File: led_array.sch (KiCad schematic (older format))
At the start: 41 parts

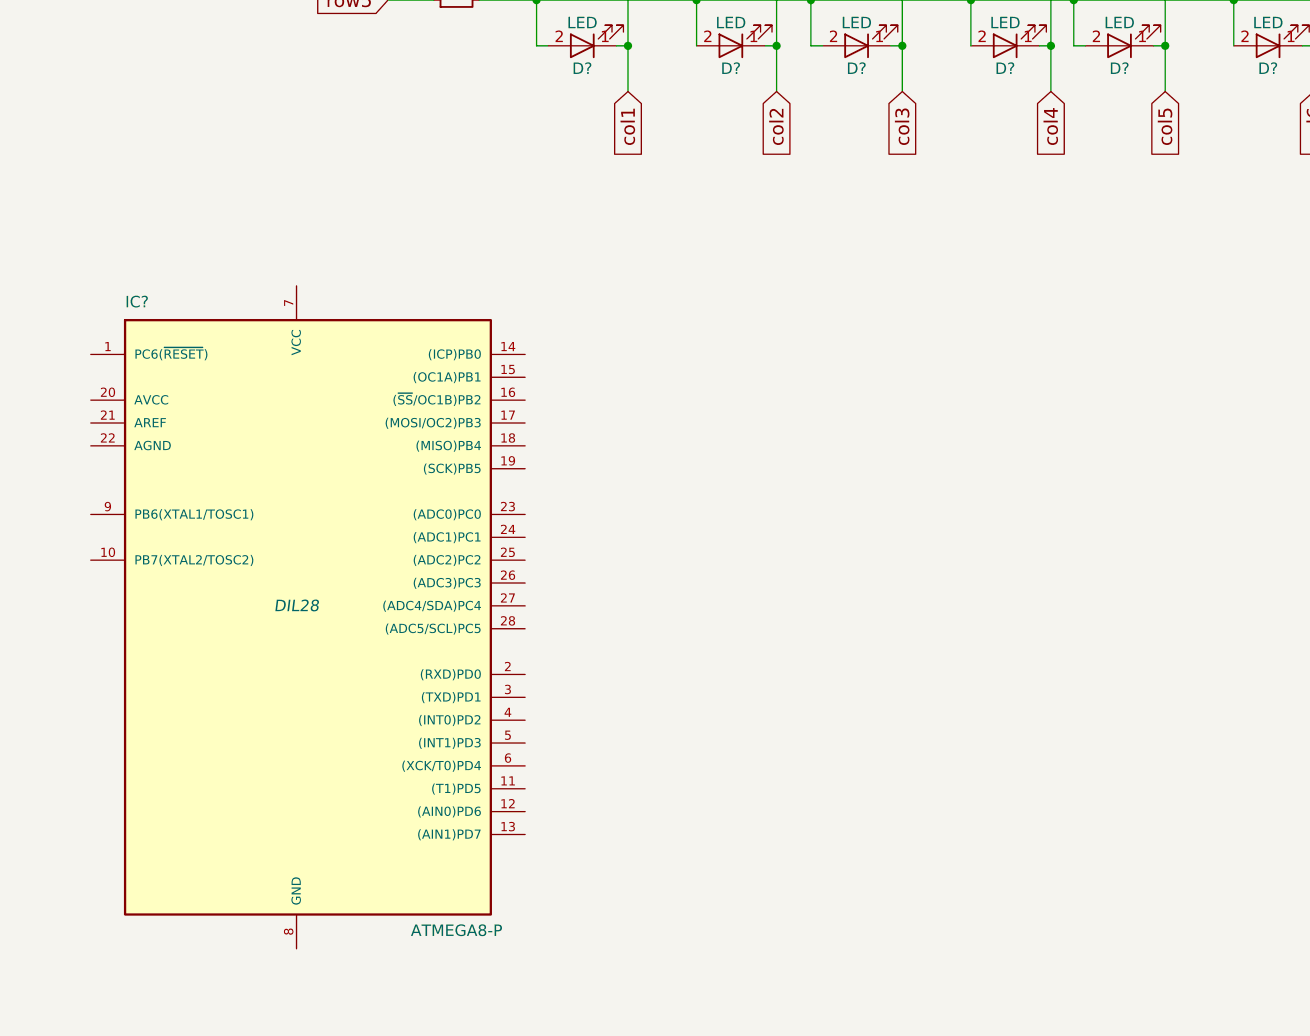
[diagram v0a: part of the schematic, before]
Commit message: Added a microcontroller atmega 8 to the project. Also added a 2X# connector to program the project
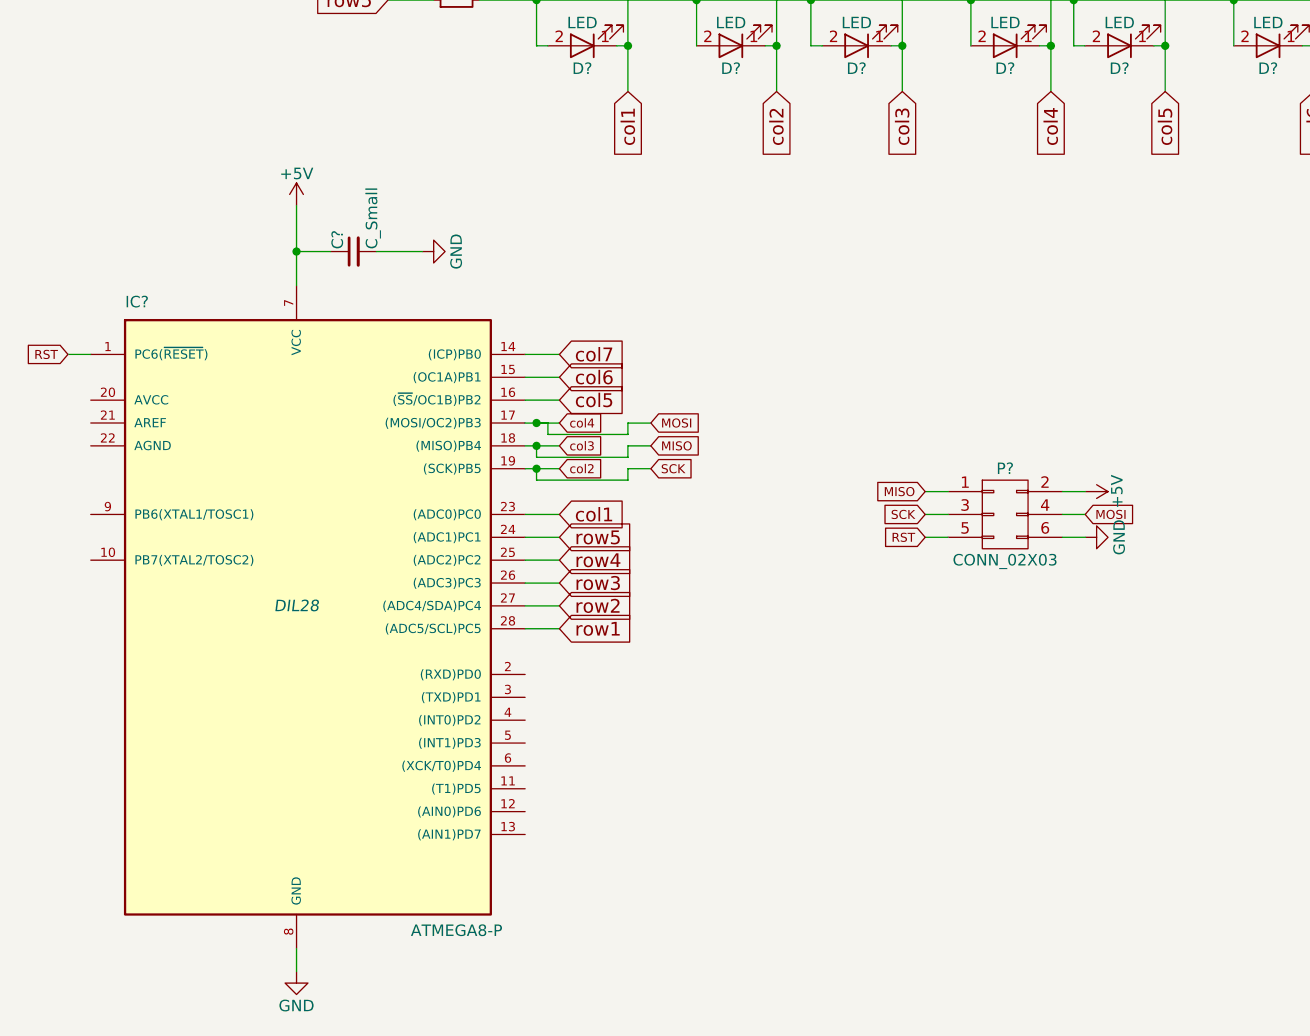
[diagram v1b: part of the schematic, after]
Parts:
- added C?: C_Small, symbol C_Small
- added P?: CONN_02X03, symbol CONN_02X03
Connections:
- net col2 is gone; now on net SCK: D?.1 (K), D?.1 (K), D?.1 (K), D?.1 (K), D?.1 (K)
- net col3 is gone; now on net MISO: D?.1 (K), D?.1 (K), D?.1 (K), D?.1 (K), D?.1 (K)
- net col4 is gone; now on net MOSI: D?.1 (K), D?.1 (K), D?.1 (K), D?.1 (K), D?.1 (K)
- net col1: now also IC?.23 ((ADC0)PC0)
- net col5: now also IC?.16 ((~SS~/OC1B)PB2)
- net col6: now also IC?.15 ((OC1A)PB1)
- net col7: now also IC?.14 ((ICP)PB0)
- net row1: now also IC?.28 ((ADC5/SCL)PC5)
- net row2: now also IC?.27 ((ADC4/SDA)PC4)
- net row3: now also IC?.26 ((ADC3)PC3)
- net row4: now also IC?.25 ((ADC2)PC2)
- net row5: now also IC?.24 ((ADC1)PC1)
- net RST: now reaches IC?.1 (PC6(~RESET~))
- net RST: now also P?.5 (P5)
- net MOSI: now reaches IC?.17 ((MOSI/OC2)PB3)
- net MOSI: now also P?.4 (P4)
- net MISO: now reaches IC?.18 ((MISO)PB4)
- net MISO: now also P?.1 (P1)
- net SCK: now reaches IC?.19 ((SCK)PB5)
- net SCK: now also P?.3 (P3)
- net +5V: now reaches IC?.7 (VCC)
- net +5V: now also C?.1, P?.2 (P2)
- net GND: now reaches IC?.8 (GND)
- net GND: now also C?.2, P?.6 (P6)
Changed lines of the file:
@@
 	1    0    0    -1
 $EndComp
+Text GLabel 3550 4450 2    60   Input ~ 0
+col7
+Text GLabel 3550 4550 2    60   Input ~ 0
+col6
+Text GLabel 3550 4650 2    60   Input ~ 0
+col5
+Text GLabel 3550 4750 2    39   Input ~ 0
+col4
+Text GLabel 3550 4850 2    39   Input ~ 0
+col3
+Text GLabel 3550 4950 2    39   Input ~ 0
+col2
+Text GLabel 3550 5150 2    60   Input ~ 0
+col1
+Text GLabel 3550 5250 2    60   Input ~ 0
+row5
+Text GLabel 3550 5350 2    60   Input ~ 0
+row4
+Text GLabel 3550 5450 2    60   Input ~ 0
+row3
+Text GLabel 3550 5550 2    60   Input ~ 0
+row2
+Text GLabel 3550 5650 2    60   Input ~ 0
+row1
+Wire Wire Line
+	3400 5650 3550 5650
+Wire Wire Line
+	3550 5550 3400 5550
+Wire Wire Line
+	3400 5450 3550 5450
+Wire Wire Line
+	3550 5350 3400 5350
+Wire Wire Line
+	3400 5250 3550 5250
+Wire Wire Line
+	3550 5150 3400 5150
+Wire Wire Line
+	3400 4950 3550 4950
+Wire Wire Line
+	3550 4850 3400 4850
+Wire Wire Line
+	3400 4750 3550 4750
+Wire Wire Line
+	3550 4650 3400 4650
+Wire Wire Line
+	3400 4550 3550 4550
+Wire Wire Line
+	3550 4450 3400 4450
+$Comp
+L CONN_02X03 P?
+U 1 1 58A9D6B0
+P 5500 5150
+F 0 "P?" H 5500 5350 50  0000 C CNN
+F 1 "CONN_02X03" H 5500 4950 50  0000 C CNN
+F 2 "" H 5500 3950 50  0000 C CNN
+F 3 "" H 5500 3950 50  0000 C CNN
+	1    5500 5150
+	1    0    0    -1
+$EndComp
+Text GLabel 5150 5050 0    39   Input ~ 0
+MISO
+Text GLabel 5150 5150 0    39   Input ~ 0
+SCK
+Text GLabel 5150 5250 0    39   Input ~ 0
+RST
+Text GLabel 5850 5150 2    39   Input ~ 0
+MOSI
+Wire Wire Line
+	5150 5050 5250 5050
+Wire Wire Line
+	5250 5150 5150 5150
+Wire Wire Line
+	5250 5250 5150 5250
+Wire Wire Line
+	5750 5150 5850 5150
+Text GLabel 3950 4850 2    39   Input ~ 0
+MISO
+Text GLabel 3950 4750 2    39   Input ~ 0
+MOSI
+Text GLabel 3950 4950 2    39   Input ~ 0
+SCK
+Wire Wire Line
+	3450 4750 3500 4750
+Wire Wire Line
+	3500 4750 3500 4800
+Wire Wire Line
+	3500 4800 3850 4800
+Wire Wire Line
+	3850 4800 3850 4750
+Wire Wire Line
+	3850 4750 3950 4750
+Connection ~ 3450 4750
+Wire Wire Line
+	3450 4850 3450 4900
+Wire Wire Line
+	3450 4900 3850 4900
+Wire Wire Line
+	3850 4900 3850 4850
+Wire Wire Line
+	3850 4850 3950 4850
+Connection ~ 3450 4850
+Wire Wire Line
+	3450 4950 3450 5000
+Wire Wire Line
+	3450 5000 3850 5000
+Wire Wire Line
+	3850 5000 3850 4950
+Wire Wire Line
+	3850 4950 3950 4950
+Connection ~ 3450 4950
+Text GLabel 1400 4450 0    39   Input ~ 0
+RST
+Wire Wire Line
+	1500 4450 1400 4450
+$Comp
+L +5V #PWR?
+U 1 1 58A9EBFC
+P 2400 3800
+F 0 "#PWR?" H 2400 3650 50  0001 C CNN
+F 1 "+5V" H 2400 3940 50  0000 C CNN
+F 2 "" H 2400 3800 50  0000 C CNN
+F 3 "" H 2400 3800 50  0000 C CNN
+	1    2400 3800
+	1    0    0    -1
+$EndComp
+Wire Wire Line
+	2400 3800 2400 4150
+$Comp
+L +5V #PWR?
+U 1 1 58A9F2C6
+P 5850 5050
+F 0 "#PWR?" H 5850 4900 50  0001 C CNN
+F 1 "+5V" H 5850 5190 50  0000 C CNN
+F 2 "" H 5850 5050 50  0000 C CNN
+F 3 "" H 5850 5050 50  0000 C CNN
+	1    5850 5050
+	0    1    1    0
+$EndComp
+Wire Wire Line
+	5850 5050 5750 5050
+$Comp
+L GND #PWR?
+U 1 1 58A9F451
+P 5850 5250
+F 0 "#PWR?" H 5850 5000 50  0001 C CNN
+F 1 "GND" H 5850 5100 50  0000 C CNN
+F 2 "" H 5850 5250 50  0000 C CNN
+F 3 "" H 5850 5250 50  0000 C CNN
+	1    5850 5250
+	0    -1   -1   0
+$EndComp
+Wire Wire Line
+	5850 5250 5750 5250
+$Comp
+L GND #PWR?
+U 1 1 58A9F7FF
+P 2400 7150
+F 0 "#PWR?" H 2400 6900 50  0001 C CNN
+F 1 "GND" H 2400 7000 50  0000 C CNN
+F 2 "" H 2400 7150 50  0000 C CNN
+F 3 "" H 2400 7150 50  0000 C CNN
+	1    2400 7150
+	1    0    0    -1
+$EndComp
+Wire Wire Line
+	2400 7150 2400 7050
+$Comp
+L C_Small C?
+U 1 1 58A9FCD3
+P 2650 4000
+F 0 "C?" H 2660 4070 50  0000 L CNN
+F 1 "C_Small" H 2660 3920 50  0000 L CNN
+F 2 "" H 2650 4000 50  0000 C CNN
+F 3 "" H 2650 4000 50  0000 C CNN
+	1    2650 4000
+	0    -1   -1   0
+$EndComp
+$Comp
+L GND #PWR?
+U 1 1 58A9FD58
+P 2950 4000
+F 0 "#PWR?" H 2950 3750 50  0001 C CNN
+F 1 "GND" H 2950 3850 50  0000 C CNN
+F 2 "" H 2950 4000 50  0000 C CNN
+F 3 "" H 2950 4000 50  0000 C CNN
+	1    2950 4000
+	0    -1   -1   0
+$EndComp
+Wire Wire Line
+	2950 4000 2750 4000
+Wire Wire Line
+	2550 4000 2400 4000
+Connection ~ 2400 4000
 $EndSCHEMATC

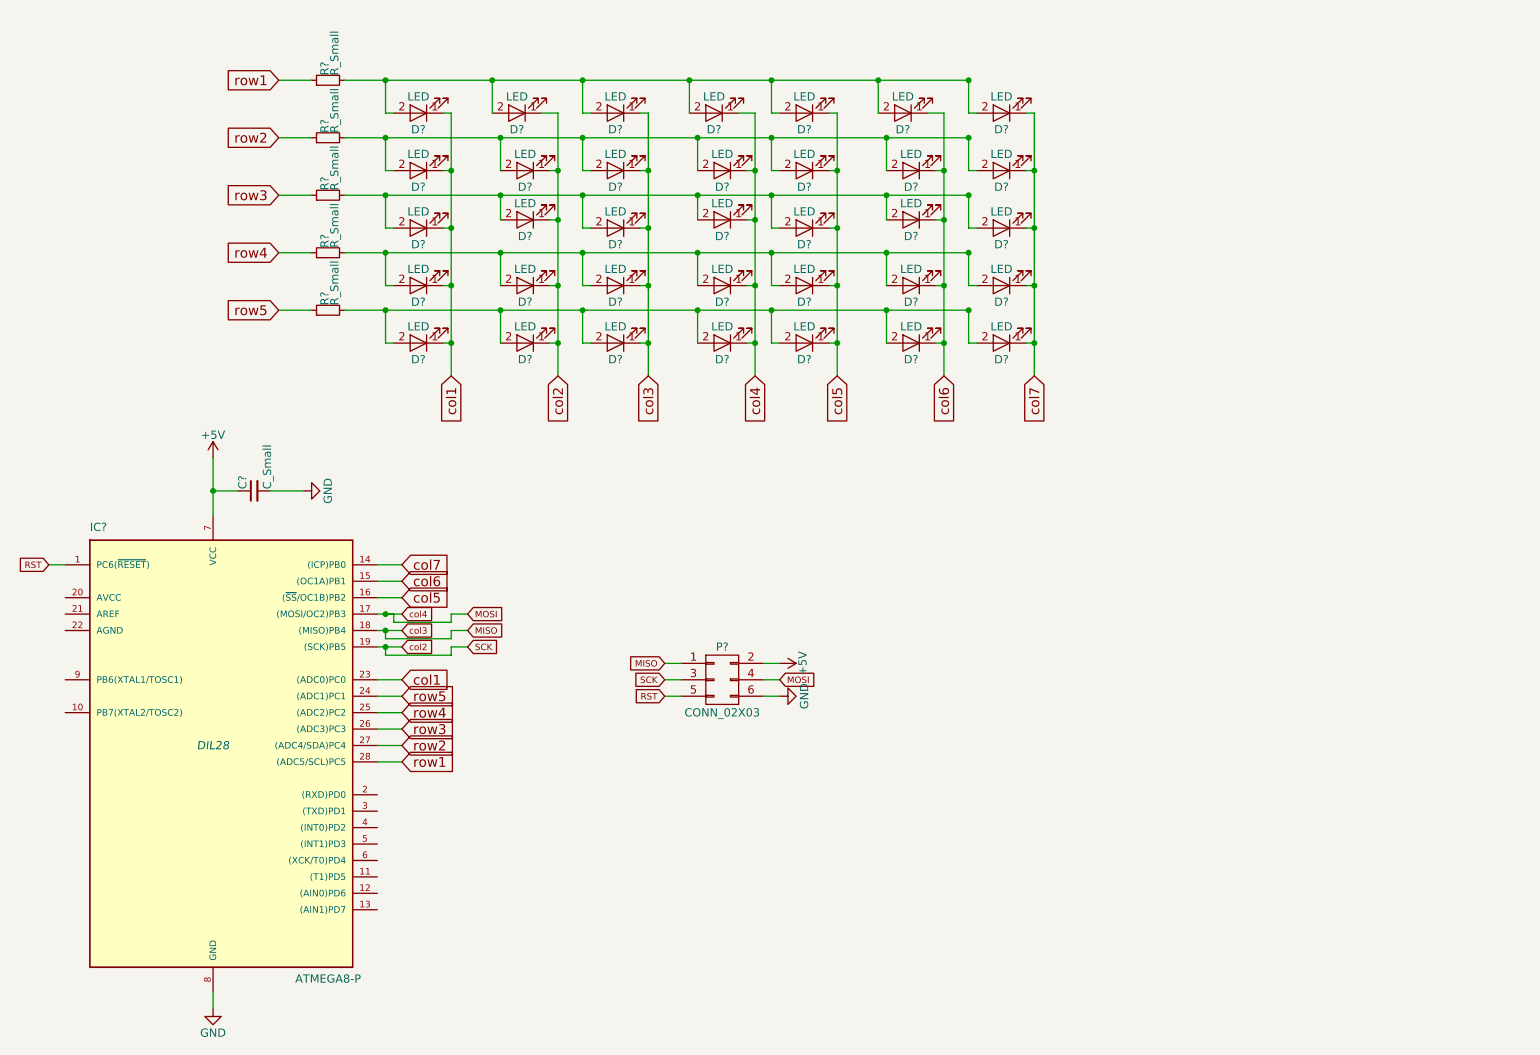
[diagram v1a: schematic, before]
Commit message: Various changes made to LED pcb
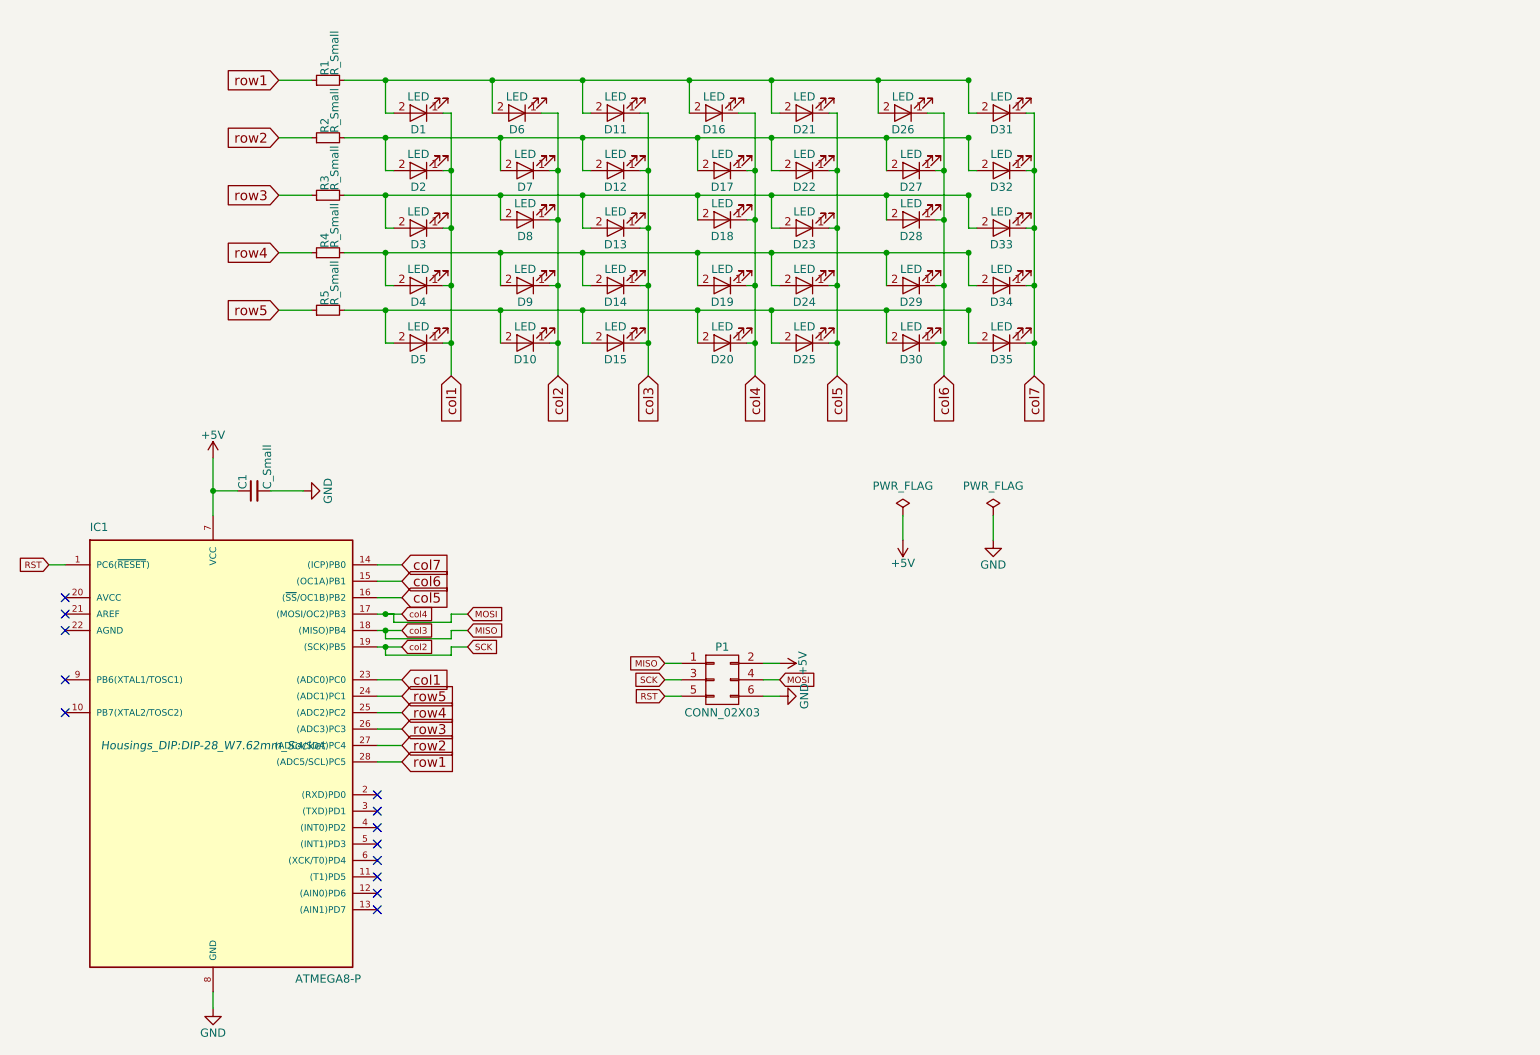
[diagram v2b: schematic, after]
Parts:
- C1: renamed from C?; footprint (none) -> Discret:C1V8
- D1, D10, D11, D12, D13, D14, D15, D16, D17, D18, D19, D2, D20, D21, D22, D23, D24, D25, D26, D27, D28, D29, D3, D30, D31, D32, D33, D34, D35, D4, D5, D6, D7, D8, D9: renamed from D?; footprint (none) -> LEDs:LED_D3.0mm
- IC1: renamed from IC?; footprint DIL28 -> Housings_DIP:DIP-28_W7.62mm_Socket
- P1: renamed from P?; footprint (none) -> Connectors:IDC_Header_Straight_6pins
- R1, R2, R3, R4, R5: renamed from R?; footprint (none) -> Discret:R3
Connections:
- no-connect marks 0 -> 13

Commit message: COmpleted routing of LEDs. Other stuff were done before this but I forgot to commit
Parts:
- added D36, D37, D38, D39, D40, D41, D42, D43, D44, D45, D46, D47, D48, D49, D50: LED, LEDs:LED_D3.0mm, symbol LED
- C1: value C_Small -> 0.1uF; footprint Discret:C1V8 -> Capacitors_THT:C_Disc_D3.0mm_W1.6mm_P2.50mm
- P1: value CONN_02X03 -> ICSP
- R1, R2, R3, R4, R5: value R_Small -> 220; footprint Discret:R3 -> Discret:R1
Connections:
- net at D1.2 (A), D11.2 (A), D16.2 (A)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: now also D36.2 (A), D41.2 (A), D46.2 (A)
- net at D12.2 (A), D17.2 (A), D2.2 (A)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: now also D37.2 (A), D42.2 (A), D47.2 (A)
- net at D13.2 (A), D18.2 (A), D23.2 (A)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: now also D38.2 (A), D43.2 (A), D48.2 (A)
- net at D14.2 (A), D19.2 (A), D24.2 (A)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: now also D39.2 (A), D44.2 (A), D49.2 (A)
- net at D10.2 (A), D15.2 (A), D20.2 (A)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: now also D40.2 (A), D45.2 (A), D50.2 (A)
- net col8: now reaches IC1.11 ((T1)PD5)
- net col8: now also D36.1 (K), D37.1 (K), D38.1 (K), D39.1 (K), D40.1 (K)
- net col9: now reaches IC1.12 ((AIN0)PD6)
- net col9: now also D41.1 (K), D42.1 (K), D43.1 (K), D44.1 (K), D45.1 (K)
- net col10: now reaches IC1.13 ((AIN1)PD7)
- net col10: now also D46.1 (K), D47.1 (K), D48.1 (K), D49.1 (K), D50.1 (K)
- net forward: now reaches IC1.4 ((INT0)PD2)
- net back: now reaches IC1.5 ((INT1)PD3)
- no-connect marks 13 -> 8

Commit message: Small changes made to the schematic
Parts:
- added J1: BARREL_JACK, Connectors:BARREL_JACK, symbol BARREL_JACK
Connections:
- net +5V: now also J1.1
- net GND: now also J1.2, J1.3
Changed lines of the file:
@@
 Wire Wire Line
 	3550 6150 3400 6150
+$Comp
+L BARREL_JACK J1
+U 1 1 58D25DE7
+P 5450 5950
+F 0 "J1" H 5450 6145 50  0000 C CNN
+F 1 "BARREL_JACK" H 5450 5795 50  0000 C CNN
+F 2 "Connectors:BARREL_JACK" H 5450 5950 50  0001 C CNN
+F 3 "" H 5450 5950 50  0001 C CNN
+	1    5450 5950
+	1    0    0    -1
+$EndComp
+$Comp
+L +5V #PWR010
+U 1 1 58D25FA4
+P 5900 5850
+F 0 "#PWR010" H 5900 5700 50  0001 C CNN
+F 1 "+5V" H 5900 5990 50  0000 C CNN
+F 2 "" H 5900 5850 50  0000 C CNN
+F 3 "" H 5900 5850 50  0000 C CNN
+	1    5900 5850
+	0    1    1    0
+$EndComp
+$Comp
+L GND #PWR011
+U 1 1 58D260AD
+P 5900 6050
+F 0 "#PWR011" H 5900 5800 50  0001 C CNN
+F 1 "GND" H 5900 5900 50  0000 C CNN
+F 2 "" H 5900 6050 50  0000 C CNN
+F 3 "" H 5900 6050 50  0000 C CNN
+	1    5900 6050
+	0    -1   -1   0
+$EndComp
+Wire Wire Line
+	5900 5850 5750 5850
+Wire Wire Line
+	5750 5950 5800 5950
+Wire Wire Line
+	5800 5950 5800 6050
+Wire Wire Line
+	5750 6050 5900 6050
+Connection ~ 5800 6050
 $EndSCHEMATC
